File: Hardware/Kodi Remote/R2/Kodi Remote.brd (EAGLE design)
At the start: 55 x 41.9 mm, 21 parts

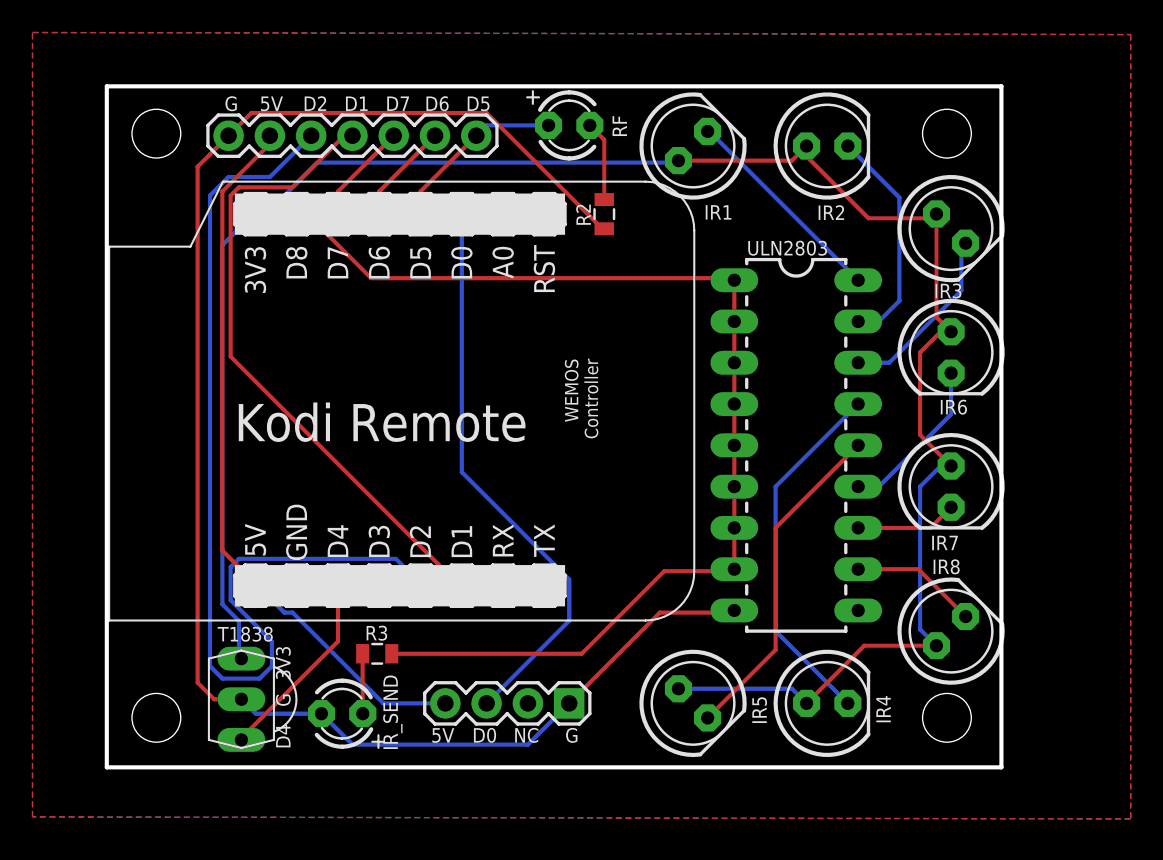
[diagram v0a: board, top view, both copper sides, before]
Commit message: Minor change to Kodi Remote
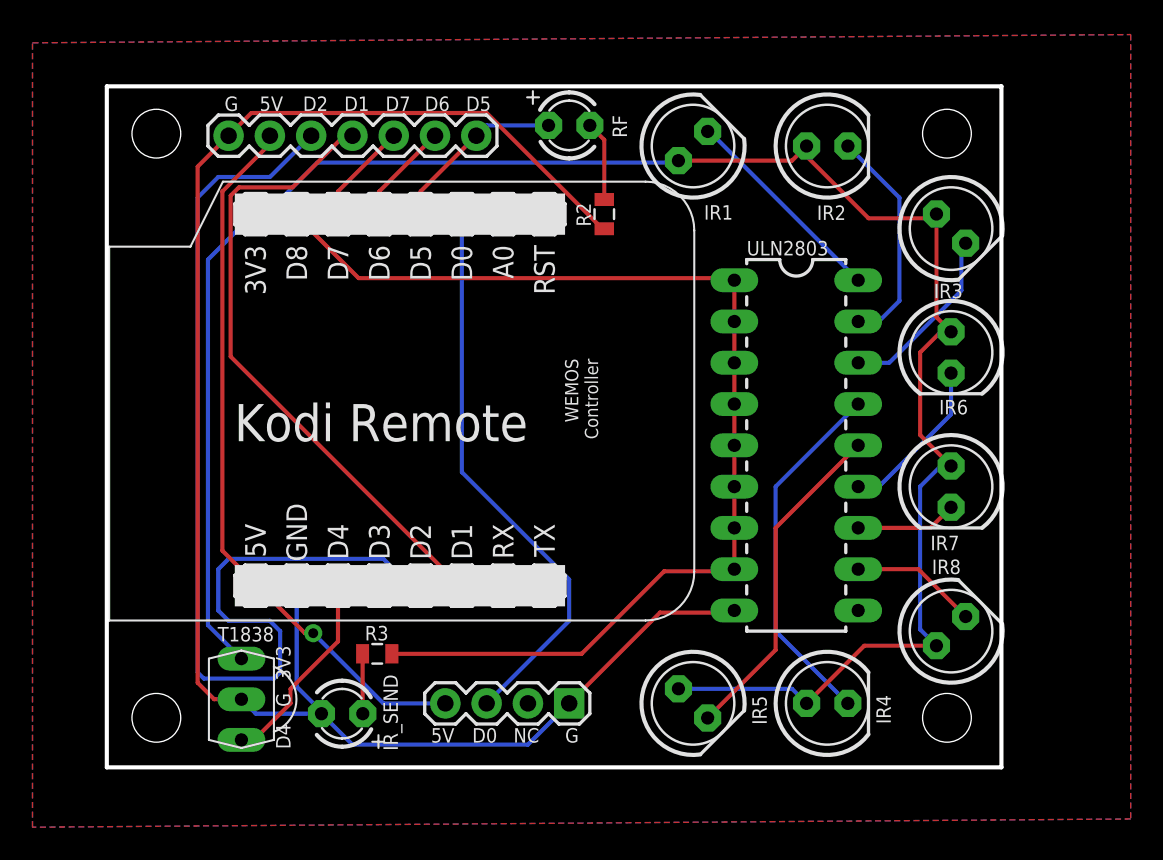
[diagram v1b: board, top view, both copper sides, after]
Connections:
- net A1 renamed A0
- net RST1 renamed RST
- net RX1 renamed RX
- net TX1 renamed TX
- removed net GND1: U$10.GND
- net GND: now also U$10.GND
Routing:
- net GND: track 99.2 -> 107.6 mm
- net D2: track 60.8 -> 65.9 mm
- net 3V3: track 122.9 -> 123.6 mm
- net 5V: vias 0 -> 1
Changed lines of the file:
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@@
 <signal name="GND">
 <polygon width="0.4064" layer="16" isolate="0.508">
-<vertex x="10.16" y="62.865"/>
+<vertex x="10.16" y="62.23"/>
 <vertex x="77.724" y="62.738"/>
 <vertex x="77.724" y="14.478"/>
-<vertex x="10.16" y="14.605"/>
+<vertex x="10.16" y="13.97"/>
 </polygon>
 <polygon width="0.4064" layer="1" isolate="0.508" thermals="no">
-<vertex x="10.16" y="62.865"/>
+<vertex x="10.16" y="62.23"/>
 <vertex x="77.724" y="62.738"/>
 <vertex x="77.724" y="14.478"/>
-<vertex x="10.16" y="14.605"/>
+<vertex x="10.16" y="13.97"/>
 </polygon>
 <contactref element="JP2" pad="1"/>
@@
 <wire x1="22.225" y1="56.515" x2="23.622" y2="57.912" width="0.254" layer="1"/>
 <wire x1="45.212" y1="50.8" x2="45.339" y2="50.789" width="0.254" layer="1"/>
-<wire x1="22.225" y1="56.515" x2="21.59" y2="55.88" width="0.254" layer="1"/>
-<wire x1="21.59" y1="55.88" x2="21.082" y2="55.372" width="0.254" layer="1"/>
 <wire x1="22.86" y1="21.844" x2="23.0136" y2="21.8428" width="0.254" layer="1"/>
 <wire x1="22.86" y1="21.844" x2="21.336" y2="21.844" width="0.254" layer="1"/>
 <wire x1="21.336" y1="21.844" x2="20.32" y2="22.86" width="0.254" layer="1"/>
 <wire x1="20.32" y1="22.86" x2="20.32" y2="54.61" width="0.254" layer="1"/>
-<wire x1="20.32" y1="54.61" x2="21.082" y2="55.372" width="0.254" layer="1"/>
+<wire x1="20.32" y1="54.61" x2="22.225" y2="56.515" width="0.254" layer="1"/>
+<contactref element="U$10" pad="GND"/>
+<wire x1="26.416" y1="22.606" x2="26.416" y2="28.702" width="0.254" layer="16"/>
+<wire x1="27.94" y1="21.082" x2="26.416" y2="22.606" width="0.254" layer="16"/>
+<wire x1="27.94" y1="21.082" x2="27.94" y2="20.955" width="0.254" layer="16"/>
 </signal>
 <signal name="N$2">
@@
 <wire x1="30.48" y1="20.955" x2="30.469" y2="24.638" width="0.254" layer="1"/>
 </signal>
-<signal name="GND1">
-<contactref element="U$10" pad="GND"/>
-</signal>
 <signal name="5V">
 <contactref element="U$10" pad="5V"/>
 <contactref element="JP2" pad="2"/>
 <contactref element="RESERVED" pad="4"/>
-<wire x1="31.75" y1="21.59" x2="35.56" y2="21.59" width="0.254" layer="16"/>
-<wire x1="26.162" y1="27.178" x2="31.75" y2="21.59" width="0.254" layer="16"/>
-<wire x1="25.654" y1="27.178" x2="26.162" y2="27.178" width="0.254" layer="16"/>
-<wire x1="23.876" y1="28.956" x2="25.654" y2="27.178" width="0.254" layer="16"/>
 <wire x1="24.638" y1="55.88" x2="24.638" y2="56.388" width="0.254" layer="1"/>
 <wire x1="21.844" y1="53.086" x2="24.638" y2="55.88" width="0.254" layer="1"/>
@@
 <wire x1="23.876" y1="28.956" x2="21.844" y2="30.988" width="0.254" layer="1"/>
 <wire x1="24.638" y1="56.388" x2="24.765" y2="56.515" width="0.254" layer="1"/>
-</signal>
-<signal name="A1">
+<wire x1="31.75" y1="21.59" x2="35.56" y2="21.59" width="0.254" layer="16"/>
+<wire x1="27.432" y1="25.908" x2="31.75" y2="21.59" width="0.254" layer="16"/>
+<wire x1="26.924" y1="25.908" x2="27.432" y2="25.908" width="0.254" layer="1"/>
+<wire x1="23.876" y1="28.956" x2="26.924" y2="25.908" width="0.254" layer="1"/>
+<via x="27.432" y="25.908" extent="1-16" drill="0.6096"/>
+</signal>
+<signal name="A0">
 <contactref element="U$10" pad="A0"/>
 </signal>
-<signal name="RST1">
+<signal name="RST">
 <contactref element="U$10" pad="RST"/>
 </signal>
-<signal name="TX1">
+<signal name="TX">
 <contactref element="U$10" pad="TX"/>
 </signal>
-<signal name="RX1">
+<signal name="RX">
 <contactref element="U$10" pad="RX"/>
 </signal>
@@
 <wire x1="53.34" y1="45.085" x2="53.34" y2="42.545" width="0.254" layer="1"/>
 <wire x1="53.34" y1="45.085" x2="53.34" y2="47.625" width="0.254" layer="1"/>
-<wire x1="27.178" y1="51.562" x2="26.416" y2="51.562" width="0.254" layer="1"/>
-<wire x1="30.988" y1="47.752" x2="27.178" y2="51.562" width="0.254" layer="1"/>
-<wire x1="53.34" y1="47.752" x2="30.988" y2="47.752" width="0.254" layer="1"/>
+<wire x1="53.34" y1="47.752" x2="30.226" y2="47.752" width="0.254" layer="1"/>
 <wire x1="53.34" y1="47.752" x2="53.34" y2="47.625" width="0.254" layer="1"/>
 <wire x1="53.34" y1="42.545" x2="53.34" y2="40.005" width="0.254" layer="1"/>
 <wire x1="32.269" y1="24.638" x2="43.942" y2="24.638" width="0.254" layer="1"/>
 <wire x1="43.942" y1="24.638" x2="49.022" y2="29.718" width="0.254" layer="1"/>
+<wire x1="30.226" y1="47.752" x2="26.416" y2="51.562" width="0.254" layer="1"/>
 </signal>
 <signal name="D0">
@@
 <wire x1="57.785" y1="21.59" x2="56.886975" y2="22.488025" width="0.254" layer="16"/>
 <wire x1="56.886975" y1="22.488025" x2="49.901971875" y2="22.488025" width="0.254" layer="16"/>
-<wire x1="22.86" y1="26.67" x2="22.86" y2="24.384" width="0.254" layer="16"/>
-<wire x1="21.844" y1="27.686" x2="22.86" y2="26.67" width="0.254" layer="16"/>
-<wire x1="21.844" y1="49.784" x2="21.844" y2="27.686" width="0.254" layer="16"/>
-<wire x1="23.876" y1="51.816" x2="21.844" y2="49.784" width="0.254" layer="16"/>
-<wire x1="22.86" y1="24.384" x2="23.0136" y2="24.3428" width="0.254" layer="16"/>
+<wire x1="23.876" y1="51.816" x2="20.955" y2="48.895" width="0.254" layer="16"/>
 <wire x1="24.638" y1="51.816" x2="23.876" y2="51.816" width="0.254" layer="16"/>
 <wire x1="27.686" y1="54.864" x2="24.638" y2="51.816" width="0.254" layer="16"/>
 <wire x1="49.784" y1="54.864" x2="27.686" y2="54.864" width="0.254" layer="16"/>
 <wire x1="49.784" y1="54.864" x2="49.901971875" y2="54.981971875" width="0.254" layer="16"/>
+<wire x1="20.955" y1="48.895" x2="20.955" y2="26.4014" width="0.254" layer="16"/>
+<wire x1="20.955" y1="26.4014" x2="23.0136" y2="24.3428" width="0.254" layer="16"/>
 </signal>
 <signal name="D1">
@@
 <contactref element="U$10" pad="D2"/>
 <contactref element="JP2" pad="3"/>
-<wire x1="21.082" y1="23.876" x2="21.082" y2="52.832" width="0.254" layer="16"/>
-<wire x1="21.844" y1="23.114" x2="21.082" y2="23.876" width="0.254" layer="16"/>
-<wire x1="24.13" y1="23.114" x2="21.844" y2="23.114" width="0.254" layer="16"/>
-<wire x1="24.892" y1="23.876" x2="24.13" y2="23.114" width="0.254" layer="16"/>
-<wire x1="24.892" y1="25.4" x2="24.892" y2="23.876" width="0.254" layer="16"/>
-<wire x1="22.352" y1="27.94" x2="24.892" y2="25.4" width="0.254" layer="16"/>
-<wire x1="22.352" y1="29.972" x2="22.352" y2="27.94" width="0.254" layer="16"/>
-<wire x1="22.86" y1="30.48" x2="22.352" y2="29.972" width="0.254" layer="16"/>
-<wire x1="32.512" y1="30.48" x2="22.86" y2="30.48" width="0.254" layer="16"/>
-<wire x1="34.036" y1="28.956" x2="32.512" y2="30.48" width="0.254" layer="16"/>
-<wire x1="21.082" y1="52.832" x2="22.225" y2="53.975" width="0.254" layer="16"/>
-<wire x1="22.225" y1="53.975" x2="24.765" y2="53.975" width="0.254" layer="16"/>
-<wire x1="24.765" y1="53.975" x2="27.305" y2="56.515" width="0.254" layer="16"/>
+<wire x1="33.274" y1="28.956" x2="34.036" y2="28.956" width="0.254" layer="16"/>
+<wire x1="31.75" y1="30.48" x2="33.274" y2="28.956" width="0.254" layer="16"/>
+<wire x1="22.225" y1="30.48" x2="31.75" y2="30.48" width="0.254" layer="16"/>
+<wire x1="20.701" y1="23.114" x2="25.019" y2="23.114" width="0.254" layer="16"/>
+<wire x1="27.305" y1="56.515" x2="24.765" y2="53.975" width="0.254" layer="16"/>
+<wire x1="21.59" y1="53.975" x2="24.765" y2="53.975" width="0.254" layer="16"/>
+<wire x1="20.701" y1="23.114" x2="20.32" y2="23.495" width="0.254" layer="16"/>
+<wire x1="20.32" y1="23.495" x2="20.32" y2="52.705" width="0.254" layer="16"/>
+<wire x1="20.32" y1="52.705" x2="21.59" y2="53.975" width="0.254" layer="16"/>
+<wire x1="22.225" y1="30.48" x2="21.59" y2="29.845" width="0.254" layer="16"/>
+<wire x1="21.59" y1="29.845" x2="21.59" y2="27.305" width="0.254" layer="16"/>
+<wire x1="21.59" y1="27.305" x2="22.225" y2="26.67" width="0.254" layer="16"/>
+<wire x1="22.225" y1="26.67" x2="24.765" y2="26.67" width="0.254" layer="16"/>
+<wire x1="25.019" y1="23.114" x2="25.4" y2="23.495" width="0.254" layer="16"/>
+<wire x1="25.4" y1="23.495" x2="25.4" y2="26.035" width="0.254" layer="16"/>
+<wire x1="25.4" y1="26.035" x2="24.765" y2="26.67" width="0.254" layer="16"/>
 </signal>
 <signal name="D3">
@@
 <contactref element="U$10" pad="D4"/>
 <contactref element="TSOP1838" pad="OUT"/>
-<wire x1="28.956" y1="25.4" x2="23.114" y2="19.558" width="0.254" layer="1"/>
 <wire x1="28.956" y1="28.956" x2="28.956" y2="25.4" width="0.254" layer="1"/>
-<wire x1="23.114" y1="19.558" x2="23.0136" y2="19.3428" width="0.254" layer="1"/>
+<wire x1="23.0136" y1="19.3428" x2="23.7878" y2="19.3428" width="0.254" layer="1"/>
+<wire x1="23.7878" y1="19.3428" x2="26.035" y2="21.59" width="0.254" layer="1"/>
+<wire x1="26.035" y1="21.59" x2="26.035" y2="22.479" width="0.254" layer="1"/>
+<wire x1="26.035" y1="22.479" x2="28.956" y2="25.4" width="0.254" layer="1"/>
 </signal>
 </signals>
